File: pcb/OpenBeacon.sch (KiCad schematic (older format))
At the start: 75 parts, among them J1 +12VDC, J2 USB_2, J3 AVR-ISP-6, J4 Ant, Q1 2N4401, Q2 2N4401, Q3 BD139-16, Q4 2N4403, Q5 2N7000, T1 FT37-43 BIFILAR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

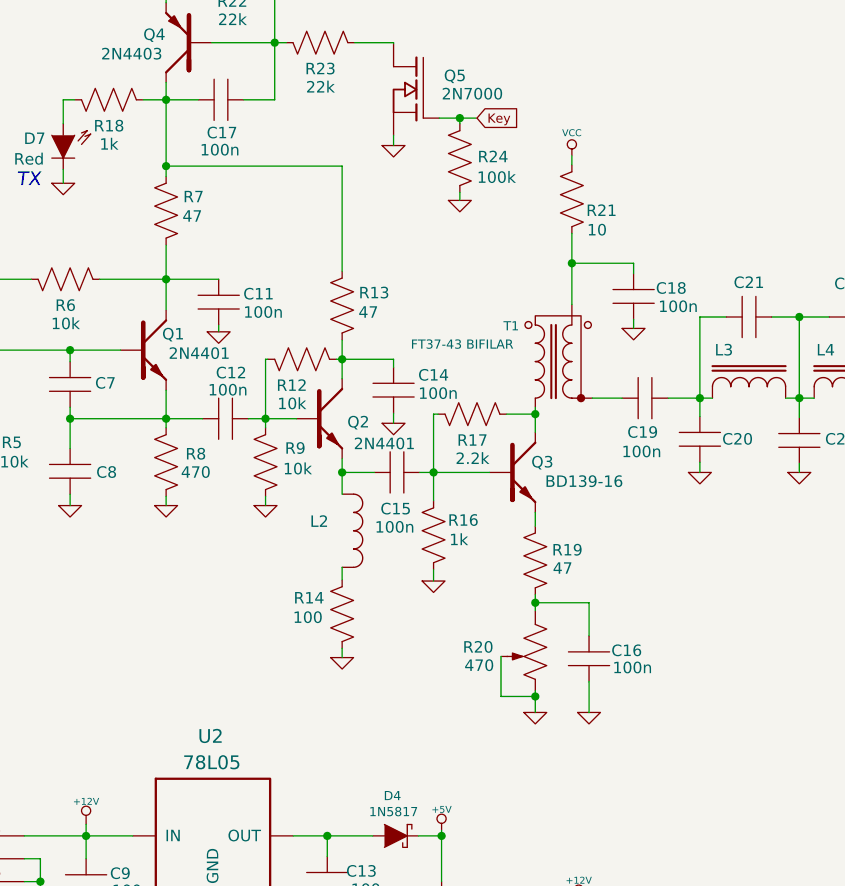
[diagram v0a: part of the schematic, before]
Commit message: Prerelease - WSPR/Glyphcode/message repeat
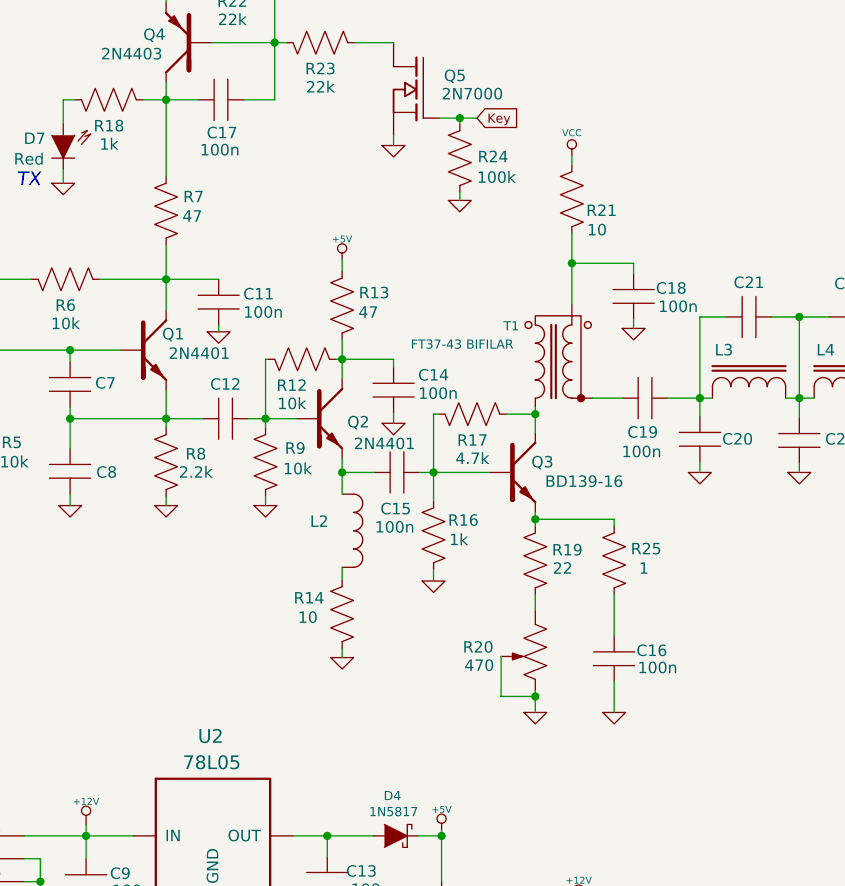
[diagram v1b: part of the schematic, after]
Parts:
- added R25: 1, symbol R
- R14: value 100 -> 10
- R17: value 2.2k -> 4.7k
- R19: value 47 -> 22
- R8: value 470 -> 2.2k
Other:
- moved on the sheet: C16

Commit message: Fix glyphcode bug, updated docs and client
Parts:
- R1, R2, R3: value 100k -> 150k
- R13: value 47 -> 10
- R14: value 10 -> 27
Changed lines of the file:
@@
-EESchema Schematic File Version 2  date Sat 07 Apr 2012 05:53:33 PM PDT
+EESchema Schematic File Version 2  date Mon 16 Apr 2012 01:52:54 PM PDT
 LIBS:NT7S
 LIBS:power
@@
 Sheet 1 1
 Title "OpenBeacon"
-Date "8 apr 2012"
+Date "16 apr 2012"
 Rev "A"
 Comp "Etherkit"
@@
 P 2345 6170
 F 0 "R1" V 2165 6155 50  0000 C CNN
-F 1 "100k" V 2240 6135 50  0000 C CNN
+F 1 "150k" V 2240 6135 50  0000 C CNN
 	1    2345 6170
 	0    1    1    0
@@
 P 2750 6170
 F 0 "R2" V 2570 6155 50  0000 C CNN
-F 1 "100k" V 2650 6135 50  0000 C CNN
+F 1 "150k" V 2650 6135 50  0000 C CNN
 	1    2750 6170
 	0    1    1    0
@@
 P 3170 6170
 F 0 "R3" V 2990 6170 50  0000 C CNN
-F 1 "100k" V 3070 6150 50  0000 C CNN
+F 1 "150k" V 3070 6150 50  0000 C CNN
 	1    3170 6170
 	0    1    1    0
@@
 P 5600 2680
 F 0 "R13" H 5740 2735 50  0000 C CNN
-F 1 "47" H 5715 2650 50  0000 C CNN
+F 1 "10" H 5715 2650 50  0000 C CNN
 	1    5600 2680
 	1    0    0    -1
@@
 P 5600 4030
 F 0 "R14" H 5455 4100 50  0000 C CNN
-F 1 "10" H 5450 4015 50  0000 C CNN
+F 1 "27" H 5450 4015 50  0000 C CNN
 	1    5600 4030
 	1    0    0    -1
@@
 P 4830 3365
 F 0 "R8" H 4960 3400 50  0000 C CNN
-F 1 "2.2k" H 4960 3320 50  0000 C CNN
+F 1 "2.2k" H 4985 3320 50  0000 C CNN
 	1    4830 3365
 	1    0    0    -1

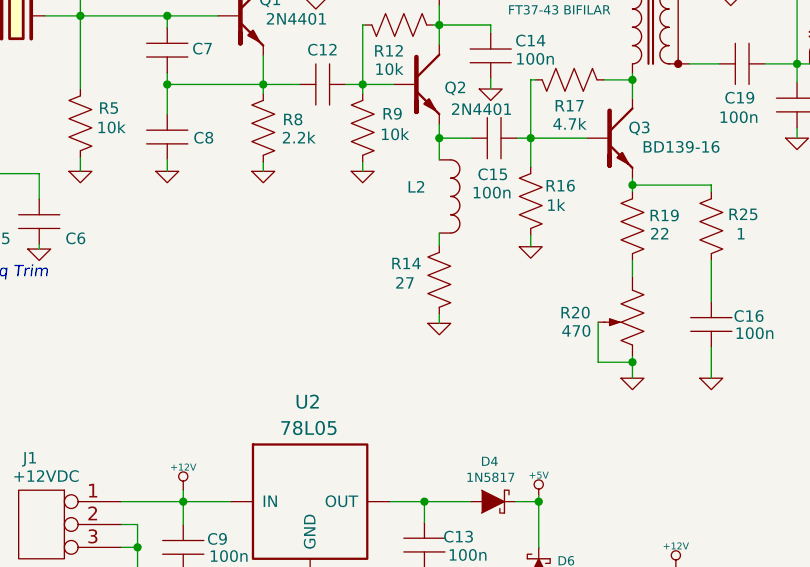
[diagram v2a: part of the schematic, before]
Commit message: Firmware bug in CW WPM, BOM corrections
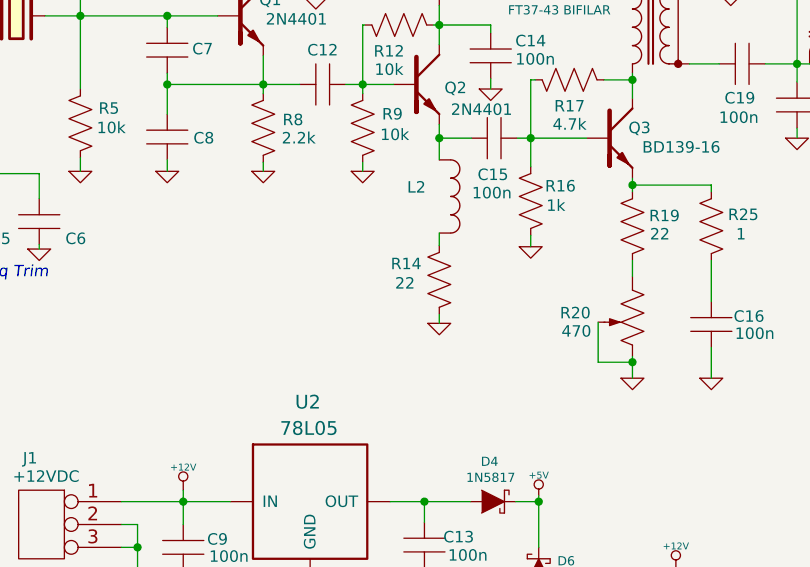
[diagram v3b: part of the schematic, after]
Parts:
- R14: value 27 -> 22
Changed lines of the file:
@@
-EESchema Schematic File Version 2  date Mon 16 Apr 2012 01:52:54 PM PDT
+EESchema Schematic File Version 2  date Thu 10 May 2012 07:23:17 PM PDT
 LIBS:NT7S
 LIBS:power
@@
 Sheet 1 1
 Title "OpenBeacon"
-Date "16 apr 2012"
+Date "11 may 2012"
 Rev "A"
 Comp "Etherkit"
@@
 P 5600 4030
 F 0 "R14" H 5455 4100 50  0000 C CNN
-F 1 "27" H 5450 4015 50  0000 C CNN
+F 1 "22" H 5450 4015 50  0000 C CNN
 	1    5600 4030
 	1    0    0    -1
